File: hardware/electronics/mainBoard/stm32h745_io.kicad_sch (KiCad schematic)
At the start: 8 parts, among them SW1 VAL, SW2 VAL, U1 STM32H745ZIT6

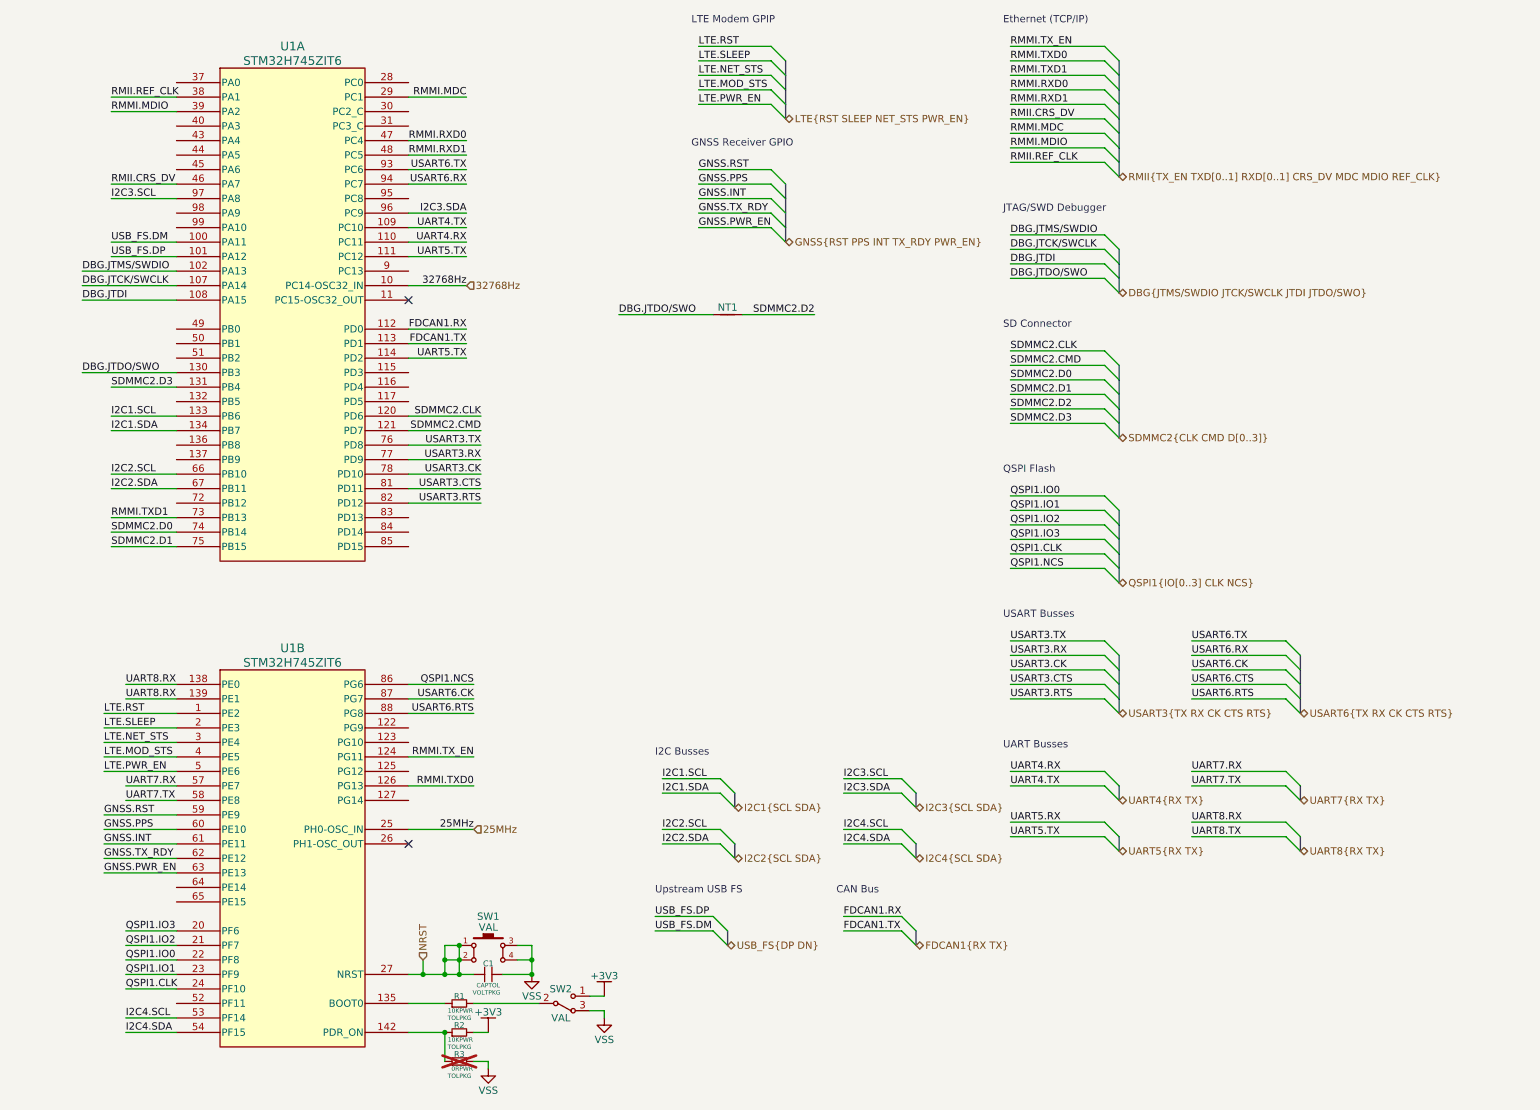
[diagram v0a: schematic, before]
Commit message: added GPIO
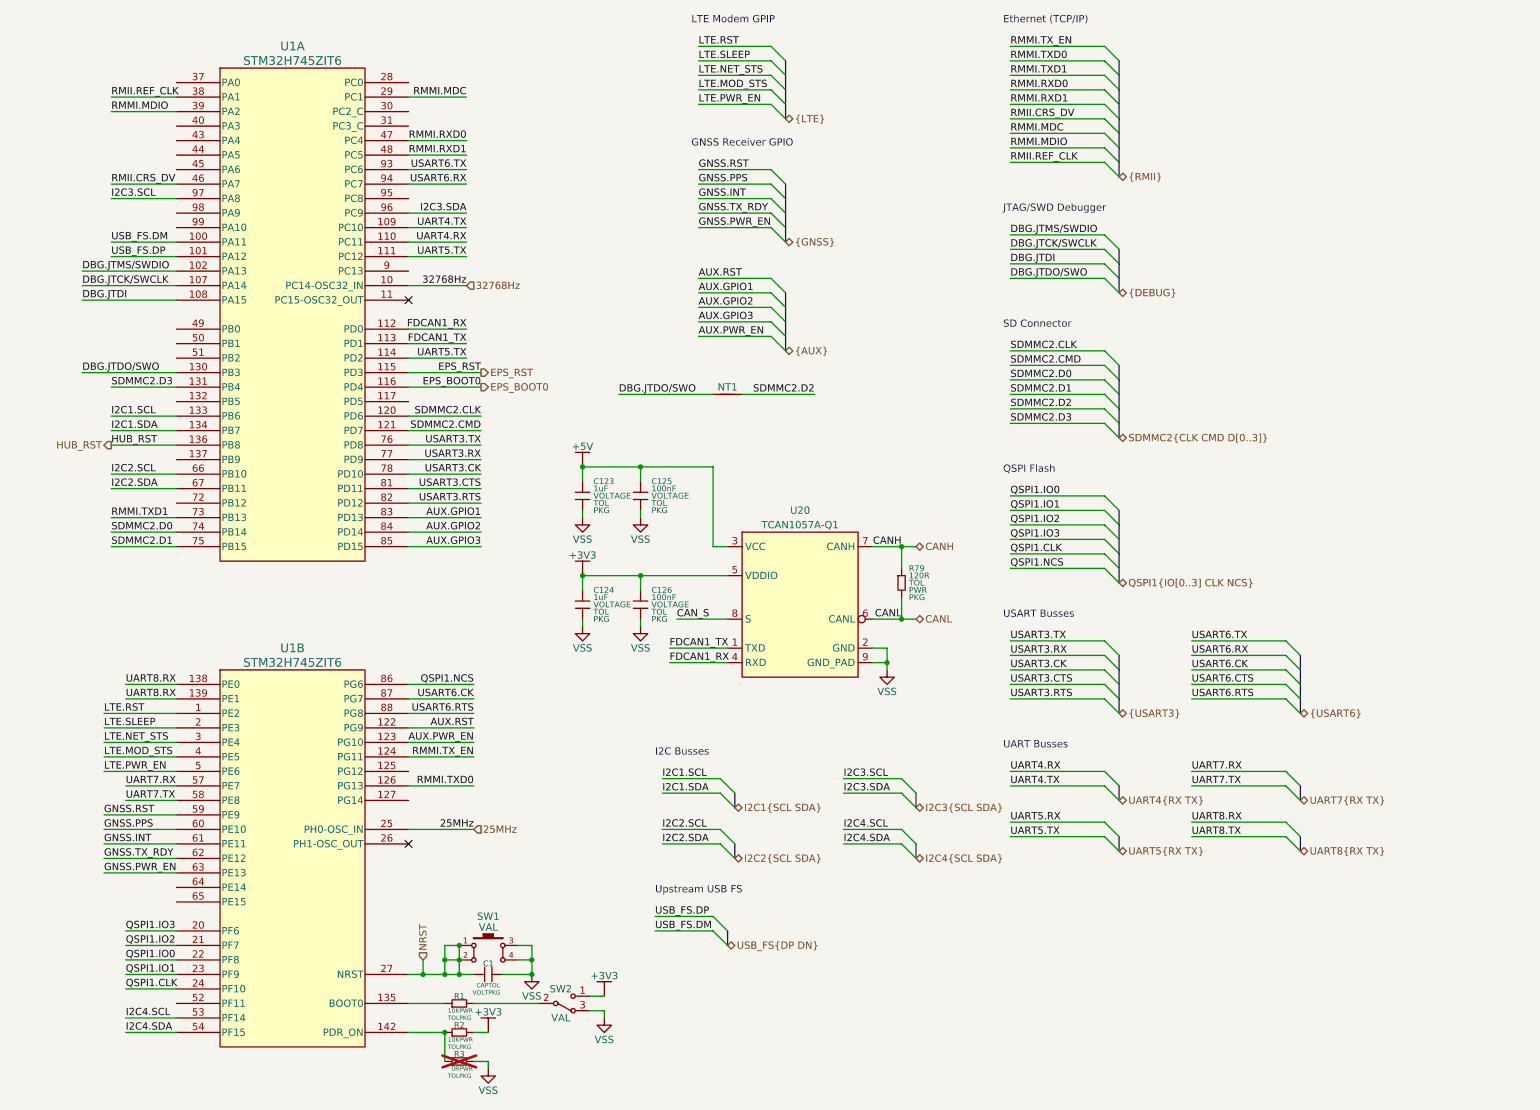
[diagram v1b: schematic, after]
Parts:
- added C123, C124: 1uF, symbol lib_sch:C
- added C125, C126: 100nF, symbol lib_sch:C
- added R79: 120R, symbol lib_sch:R
- added U20: TCAN1057A-Q1, symbol .DS-RF-Tranceivers-and-Modems:TCAN1057A-Q1
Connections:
- net +3V3: now also C124.1, C126.1, U20.5 (VDDIO)
- net VSS: now also C123.2, C124.2, C125.2, C126.2, U20.2 (GND), U20.9 (GND_PAD)
- net AUX.RST: now reaches U1.122 (PG9)
- net AUX.PWR_EN: now reaches U1.123 (PG10)
- net EPS_RST: now reaches U1.115 (PD3)
- net EPS_BOOT0: now reaches U1.116 (PD4)
- net HUB_RST: now reaches U1.136 (PB8)
- net AUX.GPIO1: now reaches U1.83 (PD13)
- net AUX.GPIO2: now reaches U1.84 (PD14)
- net AUX.GPIO3: now reaches U1.85 (PD15)
- net FDCAN1.RX renamed FDCAN1_RX
- net FDCAN1_RX: now also U20.4 (RXD)
- net FDCAN1.TX renamed FDCAN1_TX
- net FDCAN1_TX: now also U20.1 (TXD)
- new net +5V: C123.1, C125.1, U20.3 (VCC)
- new net CANH: R79.1, U20.7 (CANH)
- new net CANL: R79.2, U20.6 (CANL)
- new net CAN_S: U20.8 (S)
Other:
- note removed: "CAN Bus"
- moved on the sheet: NT1

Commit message: fixed nets
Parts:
- removed C124: 1uF, symbol lib_sch:C
- removed C126: 100nF, symbol lib_sch:C
- removed R1: 10K, symbol lib_sch:R_horizontal
- removed SW2: VAL, symbol lib_sch:SPDT
- added C2: 100nF, symbol lib_sch:C_horizontal
- added C5: 1uF, symbol lib_sch:C
- added C6: 100nF, symbol lib_sch:C
- added D1: D1213A-01LP4, symbol lib_sch:D_TVS_single_horizontal
- added R1, R3: 10K, symbol lib_sch:R
- added R10, R11, R12, R5, R6, R7, R8, R9: 4K7, symbol lib_sch:R
- added SW2: PTS810, symbol lib_sch:SPST-NO Button
- C1: value CAP -> 100nF; DKPN (none) -> 478-KAM15AR71H104KTCT-ND; MPN (none) -> 06035C104K4T2A; Manufacturer (none) -> KYOCERA AVX; Package PKG -> 0603; Tolerace TOL -> (none); Tolerance (none) -> 10%; Voltage Rating VOLT -> 50V
- C3: renamed from C123; DKPN (none) -> 478-KAM15AR71A105KTCT-ND; MPN (none) -> KAM15AR71A105KT; Manufacturer (none) -> KYOCERA AVX; Package PKG -> 0603; Tolerance TOL -> 10%; Voltage Rating VOLTAGE -> 10V
- C4: renamed from C125; DKPN (none) -> 478-KAM15AR71H104KTCT-ND; MPN (none) -> 06035C104K4T2A; Manufacturer (none) -> KYOCERA AVX; Package PKG -> 0603; Tolerance TOL -> 10%; Voltage Rating VOLTAGE -> 50V
- R13: renamed from R79; DKPN (none) -> 541-120LCT-ND; MPN (none) -> CRCW0402120RFKED; Manufacturer (none) -> Vishay Dale; Package PKG -> 0402; Power Rating PWR -> 62m5W; Tolerance TOL -> 1%
- R2: DKPN (none) -> 541-10.0KLCT-ND; MPN (none) -> CRCW040210K0FKED; Manufacturer (none) -> Vishay Dale; Package PKG -> 0402; Power Rating PWR -> 62m5W; Tolerance TOL -> 1%
- R4: renamed from R3; DKPN (none) -> 541-0.0JCT-ND; MPN (none) -> CRCW04020000Z0ED; Manufacturer (none) -> Vishay Dale; Package PKG -> 0402; Power Rating PWR -> 62m5W; Tolerance TOL -> N/A
- SW1: value VAL -> PTS810; DKPN (none) -> CKN10502CT-ND; MPN (none) -> PTS810SJM250SMTR LFS; Manufacturer (none) -> C&K
- U1: footprint LQFP-144 -> (none); DKPN (none) -> 497-19501-ND; MPN (none) -> STM32H745ZIT6; Manufacturer (none) -> STMicroelectronics
- U2: renamed from U20; symbol .DS-RF-Tranceivers-and-Modems:TCAN1057A-Q1 -> lib_sch:TCAN1057A-Q1; DKPN (none) -> 296-TCAN1057ADRBRQ1CT-ND; MPN (none) -> TCAN1057ADRBRQ1
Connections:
- net RMMI.TXD0 is gone; now on net USART6.CTS: U1.126 (PG13)
- net +3V3: now also C5.1, C6.1, R1.1, R10.1, R11.1, R12.1, R5.1, R6.1, R7.1, R8.1, R9.1
- net CAN_S: now also U1.99 (PA10)
- net I2C1.SCL: now also R5.2
- net I2C1.SDA: now also R6.2
- net I2C2.SCL: now also R7.2
- net I2C2.SDA: now also R8.2
- net I2C3.SCL: now also R9.2
- net I2C3.SDA: now also R10.2
- net I2C4.SCL: now also R11.2
- net I2C4.SDA: now also R12.2
- net NRST: now also D1.2
- net UART5.RX: now also U1.114 (PD2)
- net UART5.TX: no longer U1.114 (PD2)
- net UART8.RX: no longer U1.139 (PE1)
- net UART8.TX: now also U1.139 (PE1)
- net VSS: now also C5.2, C6.2, D1.1, R3.2
- net EEPROM_WC: now reaches U1.127 (PG14)
- net STM32H7_BOOT0: now reaches U1.135 (BOOT0)
- net STM32H7_BOOT0: now also C2.1, R3.1, SW2.1, SW2.2
- net PDR_ON: now reaches R2.1, R4.1, U1.142 (PDR_ON)
- net RMII.TXD0: now reaches U1.72 (PB12)
- net RMMI.MDC renamed RMII.MDC
- net RMMI.MDIO renamed RMII.MDIO
- net RMMI.RXD0 renamed RMII.RXD0
- net RMMI.RXD1 renamed RMII.RXD1
- net RMMI.TXD1 renamed RMII.TXD1
- net RMMI.TX_EN renamed RMII.TX_EN
- net USART3.CK: no longer names the net of U1.78 (PD10)
- net USART6.CK: no longer names the net of U1.87 (PG7)
- net USB_FS.DM renamed USB_FS.DN
- new net: C2.2, R1.2, SW2.3, SW2.4
- no-connect marks 2 -> 25
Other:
- note added: "AUX Card GPIO"
- note added: "CANBus Transceiver"
- moved on the sheet: C1, C3, C4, NT1, R13, R2, R4, SW1, U1A, U1B, U2
